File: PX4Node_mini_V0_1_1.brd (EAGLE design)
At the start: 48.6 x 34.9 mm, 127 parts, among them J2 DF13-4P-1.25V, J201 DF13C-6P-1.25V, J202 DF13C-6P-1.25V, J203 DF13C-6P-1.25V, J3 DF13C-4P-1.25V, J302 DF13C-4P-1.25V, J401 DF13C-4P-1.25V, J403 DF13C-7P-1.25V, J405 DF13C-4P-1.25V, J802 DF13C-3P-1.25V, M3_MOUNT1101 MOUNT-HOLE3.1MM, M3_MOUNT1102 MOUNT-HOLE3.1MM, M3_MOUNT1103 MOUNT-HOLE3.1MM, M3_MOUNT1104 MOUNT-HOLE3.1MM, U101 STM32F4X7VX, U2 MAX3051, U401 MAX3051, X101 3.2x2.5 mm / 24 MHz / 15 ppm

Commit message: Some tweaks
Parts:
- added SJ3: SOLDERJUMPERNO, SparkFun-Passives:SJ_2S-NO
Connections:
- new net 5V_CAN_CONN: L403.P$1, L7.P$1, SJ3.2
- net VDD_5V_PERIPH: now also SJ3.1; no longer L403.P$1, L7.P$1
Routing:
- net 5V_CAN_CONN: track 0.00 -> 24.1 mm, vias 0 -> 3
- net VDD_5V_PERIPH: track 85.7 -> 66.3 mm, vias 19 -> 17
- net GND: track 231.8 -> 227.8 mm
- net VDD_3V3_SENSORS_EN: track 34.2 -> 36.7 mm, vias 3 -> 2

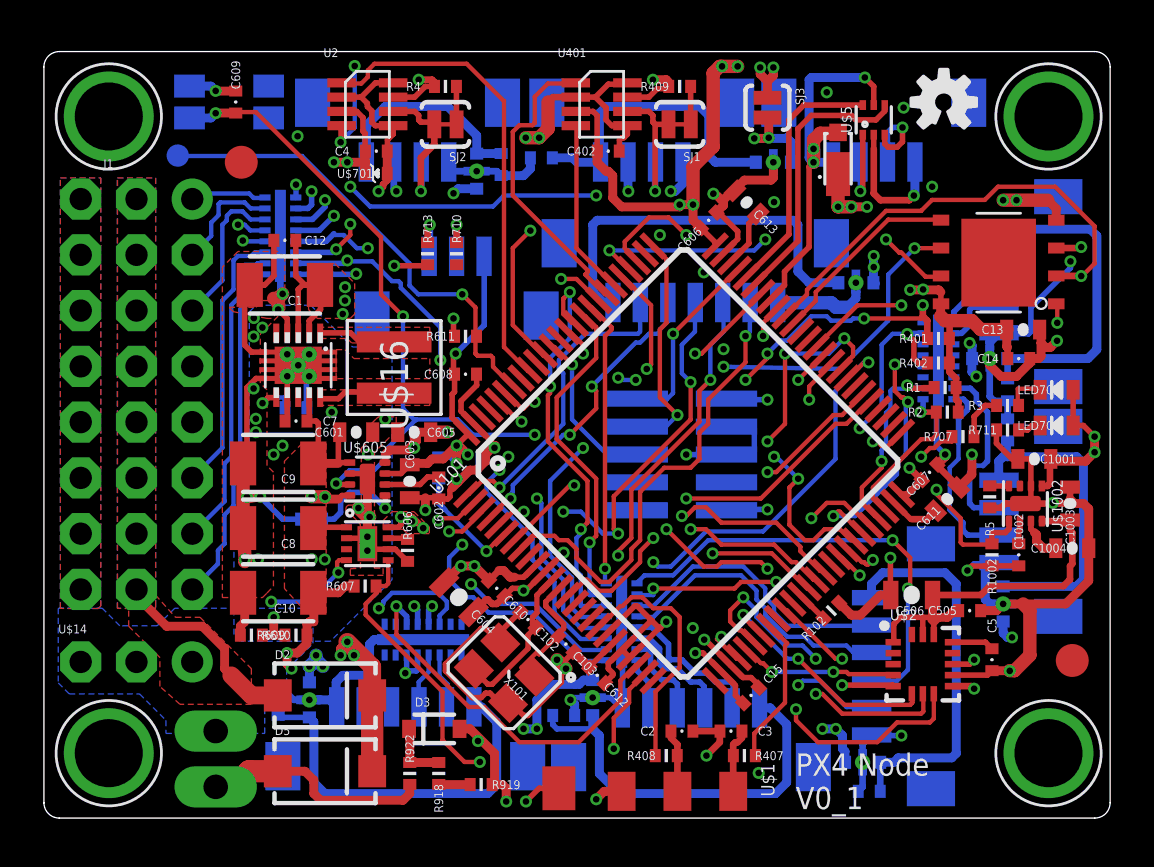
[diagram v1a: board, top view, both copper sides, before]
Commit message: Tweaks to power and grounds
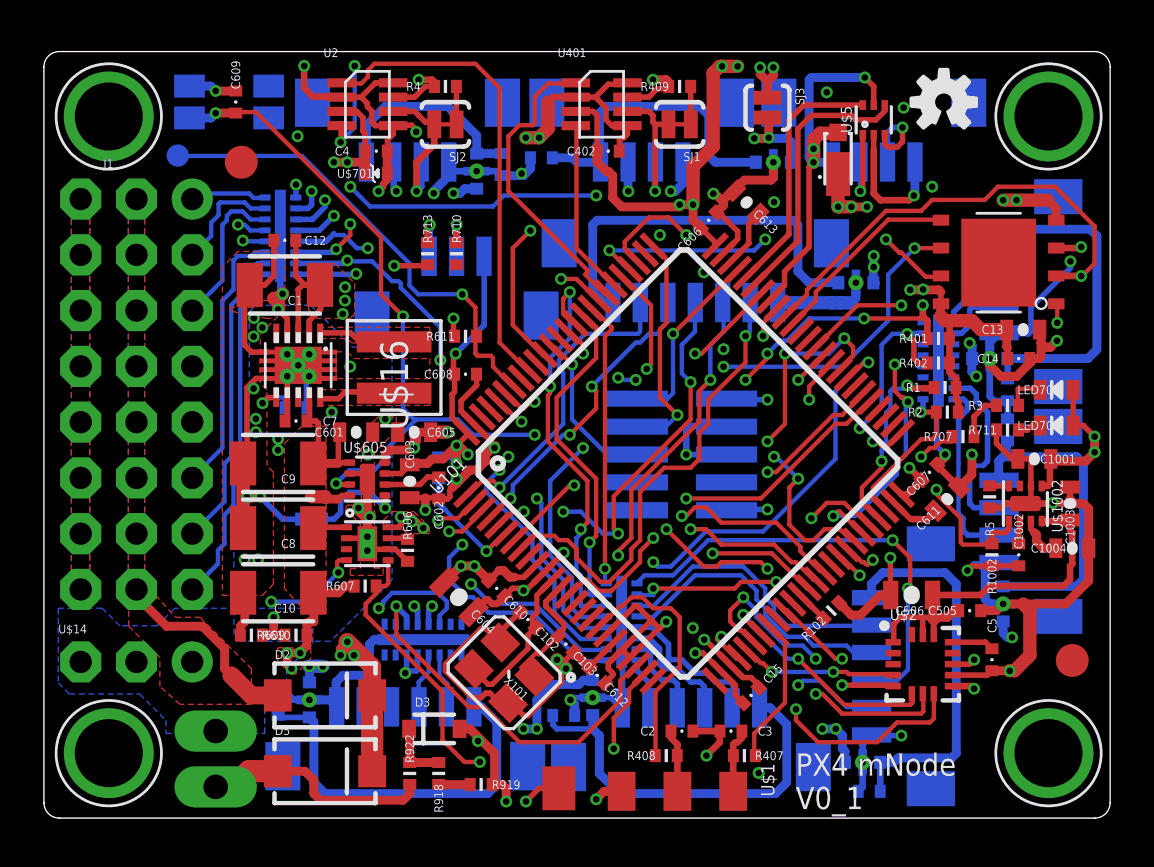
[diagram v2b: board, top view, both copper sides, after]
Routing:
- net GND: track 227.8 -> 230.8 mm, vias 52 -> 57
- net VDD_5V_PERIPH: track 66.3 -> 65.2 mm, vias 17 -> 16
- net VDD_5V: track 80.1 -> 80.2 mm, vias 8 -> 5
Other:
- board text added: "PX4 mNode V0_1"
- board text removed: "PX4 Node V0_1"
